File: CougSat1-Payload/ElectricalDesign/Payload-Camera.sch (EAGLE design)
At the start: 57 parts, among them J1 CougSat Card, U1 AD7291, U2 AD8515, U3 AD8616, U4 AD8515, U5 CD74HC4040M, U6 TPS73250, U7 TPS61220, U8 TCA9535R

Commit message: Final asthetic changes, exported pdf
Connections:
- net N$1 renamed PD_IN
- net N$10 renamed TEMP_7
- net N$11 renamed PD_VDIV_OUT
- net N$12 renamed DIFF_INT_IN
- net N$13 renamed DIFF_IN
- net N$14 renamed TEMP_0
- net N$15 renamed DIFF_OUT
- net N$16 renamed TEMP_2
- net N$17 renamed PD_OUTD
- net N$18 renamed COUNTER_RESET
- net N$2 renamed CAMP_IN
- net N$21 renamed COUNT_1
- net N$25 renamed COUNT_2
- net N$26 renamed COUNT_3
- net N$27 renamed COUNT_4
- net N$28 renamed COUNT_5
- net N$29 renamed COUNT_6
- net N$3 renamed PD_OUT_THRESH
- net N$30 renamed COUNT_7
- net N$31 renamed COUNT_8
- net N$32 renamed COUNT_9
- net N$33 renamed COUTN_10
- net N$34 renamed COUNT_11
- net N$35 renamed COUNT_12
- net N$4 renamed TEMP_1
- net N$5 renamed CAMP_OUT
- net N$6 renamed TEMP_3
- net N$7 renamed TEMP_4
- net N$8 renamed TEMP_5
- net N$9 renamed TEMP_6
- net !CS-TELEPHOTO: now also J1GPIO.GPIO-0
- net !CS-WIDE_ANGLE: now also J1GPIO.GPIO-1
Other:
- note added: "3C2>"
- note added: "3C6> 4A3> 4A5>"
- note added: "4A3>"
- note added: "4A3> 4A5>"
- note added: "4A5>"
- note added: "<3B2"
- note added: "<3B2>"
- note added: "<3C2"
- note added: "<3C2>"
- note added: "<3C6> <4A3> <4A5>"
- note added: "<4A3 <4A5"
- note added: "<4B2"
- note added: "<4B2>"
- note added: "Page 1: Block Diagram Page 2: Power Rails Page 3: Connector/ADC Page 4: Geiger Counter, Cameras Page 4: Mechanical"
- note added: "Page 3"
- note added: "Page 4"
- note removed: "3xx>"
- note removed: "3xx> 4\xx> 4xx>"
- note removed: "4xx>"
- note removed: "4xx> 4xx>"
- note removed: "<3xx"
- note removed: "<3xx>"
- note removed: "<3xx> <4xx> <4xx>"
- note removed: "<4xx"
- note removed: "<4xx <4xx"
- note removed: "<4xx>"
- note removed: "Page 1: Block Diagram Page 2: Power Rails Page 3: Connector/ADC/Cameras Page 4: Geiger Counter Page 4: Mechanical"

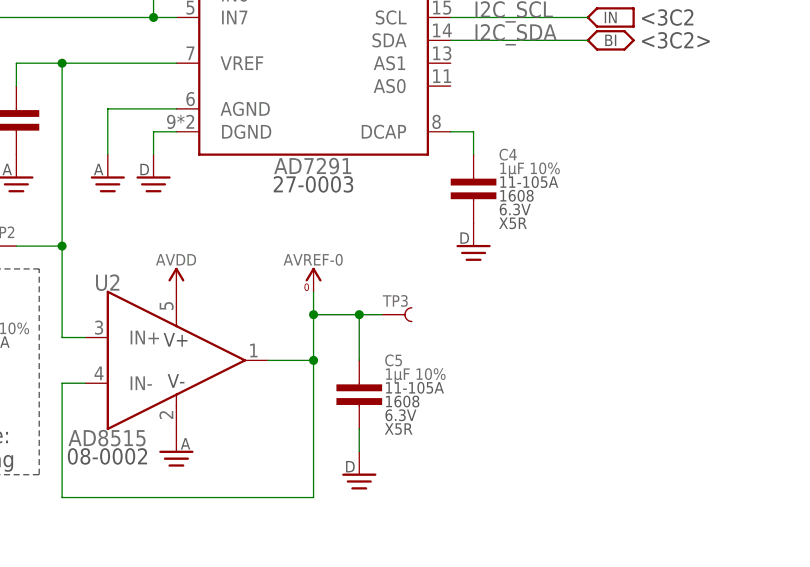
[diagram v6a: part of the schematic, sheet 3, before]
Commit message: Document block diagram section
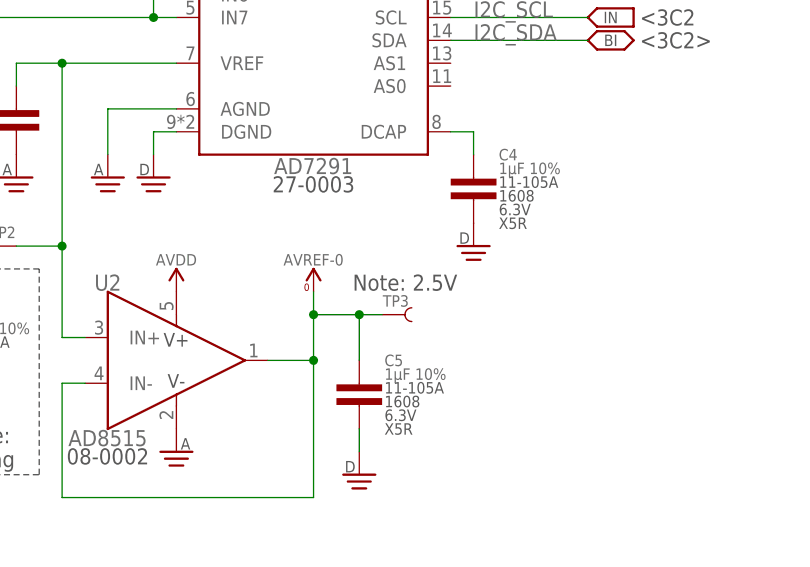
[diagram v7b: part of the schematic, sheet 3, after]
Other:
- note added: "Note: 2.5V"
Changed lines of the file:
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@@
 <setting verticaltext="up"/>
 </settings>
-<grid distance="0.1" unitdist="inch" unit="inch" style="lines" multiple="1" display="no" altdistance="0.05" altunitdist="inch" altunit="inch"/>
+<grid distance="0.1" unitdist="inch" unit="inch" style="lines" multiple="1" display="no" altdistance="0.01" altunitdist="inch" altunit="inch"/>
 <layers>
 <layer number="1" name="Top" color="4" fill="1" visible="no" active="no"/>
@@
 <text x="71.12" y="55.88" size="1.778" layer="97" align="center-left"> 4A3&gt;</text>
 <text x="71.12" y="53.34" size="1.778" layer="97" align="center-left"> 4A5&gt;</text>
+<text x="203.2" y="56.896" size="1.778" layer="97" align="center">Note: 2.5V</text>
 </plain>
 <instances>

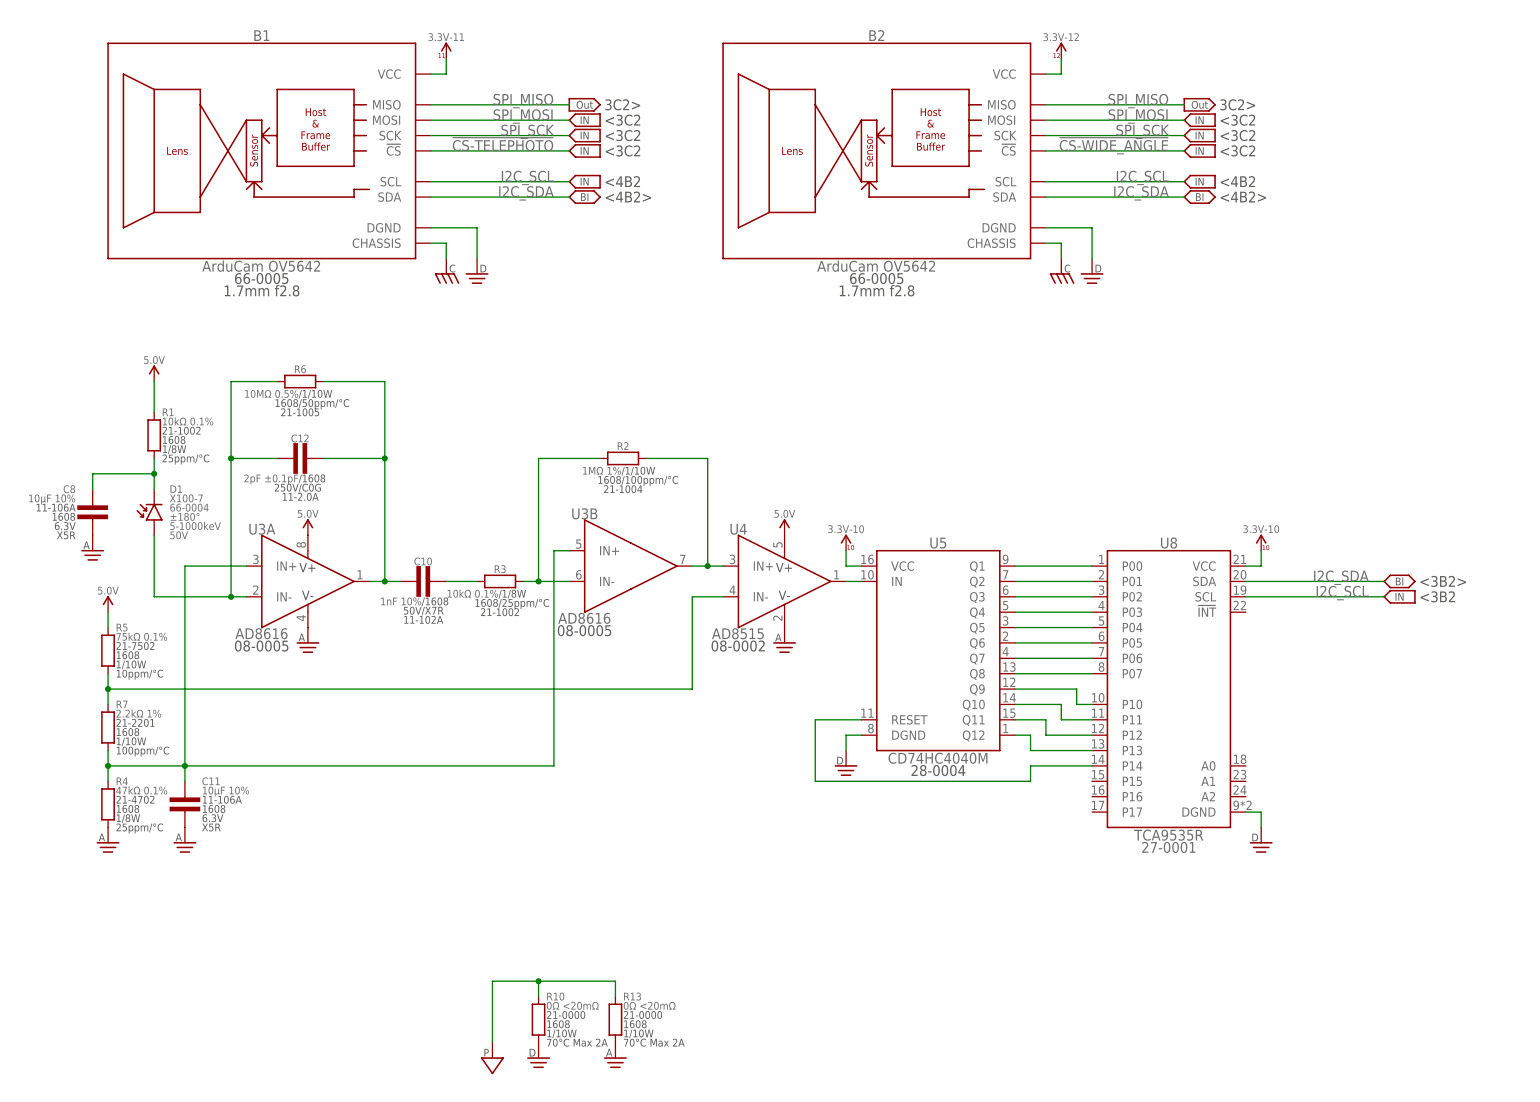
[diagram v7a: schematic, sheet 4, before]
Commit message: Added dcaps, wrote more documentation
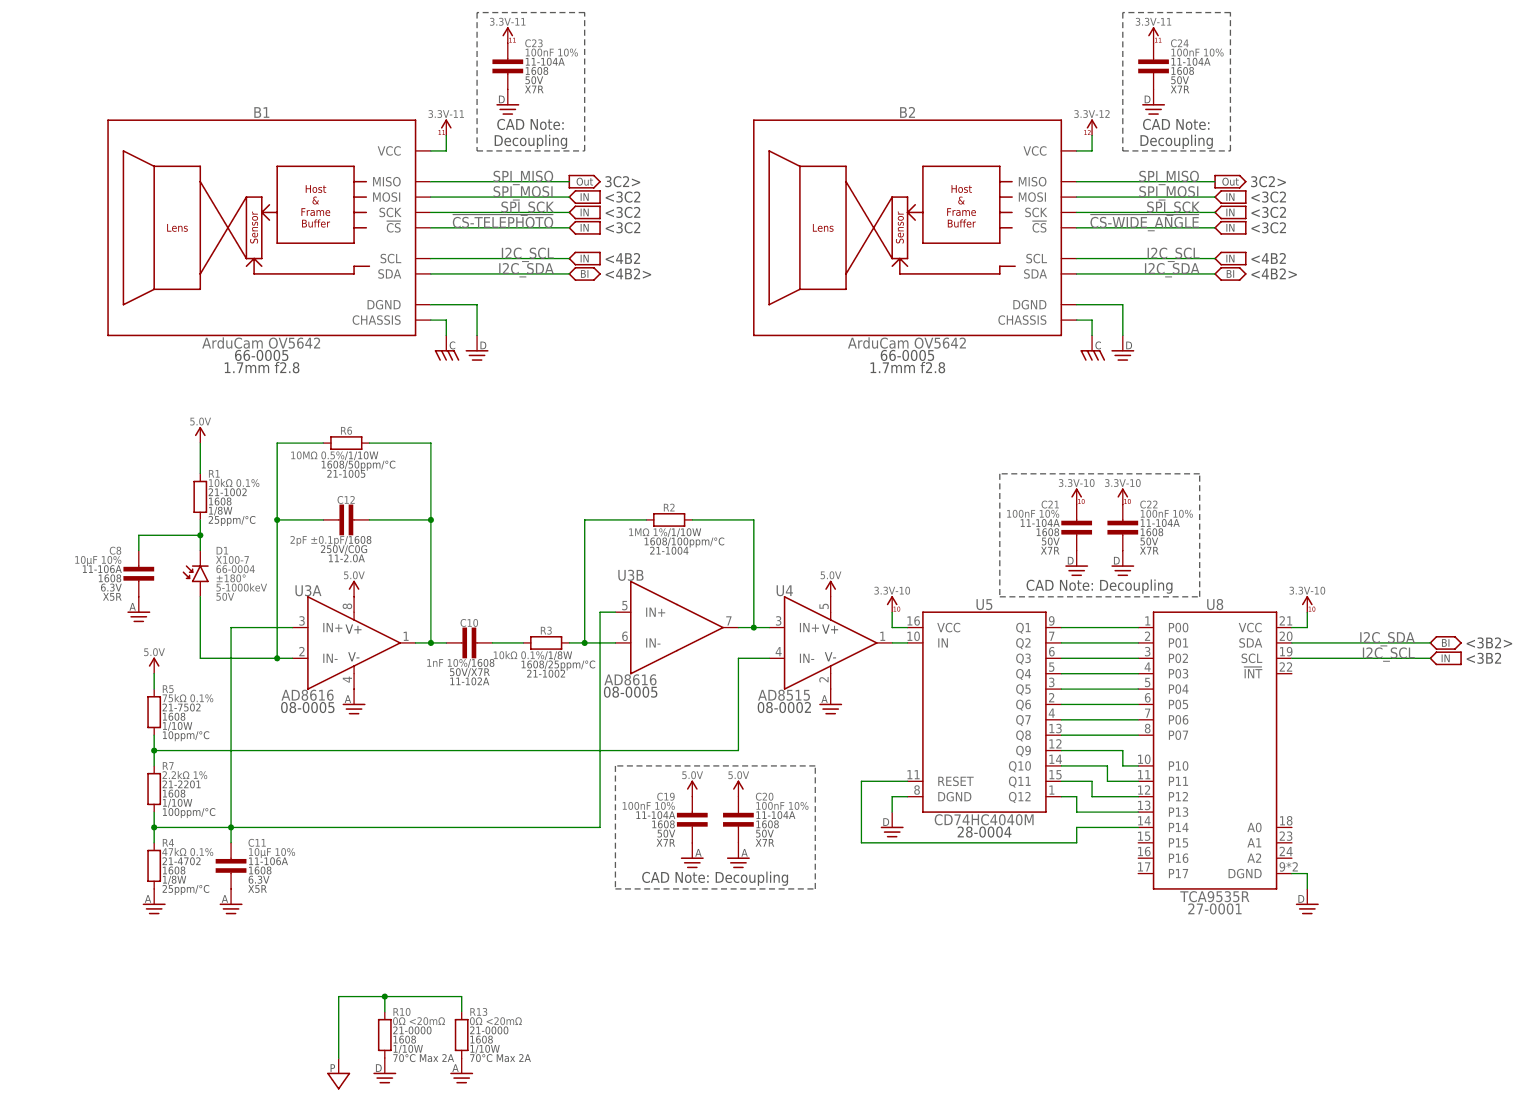
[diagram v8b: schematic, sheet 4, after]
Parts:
- added C19, C20, C21, C22, C23, C24: 100nF 10%, CougsInSpace-Capacitors:CAP-V-100NF-1608
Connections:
- net 3.3V_10: now also C21.1, C22.1
- net 3.3V_11: now also C23.1, C24.1
- net 5.0V: now also C19.1, C20.1
- net AGND: now also C19.2, C20.2
- net DGND: now also C21.2, C22.2, C23.2, C24.2
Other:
- moved on the sheet: B1, B2, C10, C11, C12, C8, D1, R1, R10, R13, R2, R3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
